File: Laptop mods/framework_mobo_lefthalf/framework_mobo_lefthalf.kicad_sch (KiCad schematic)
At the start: 19 parts

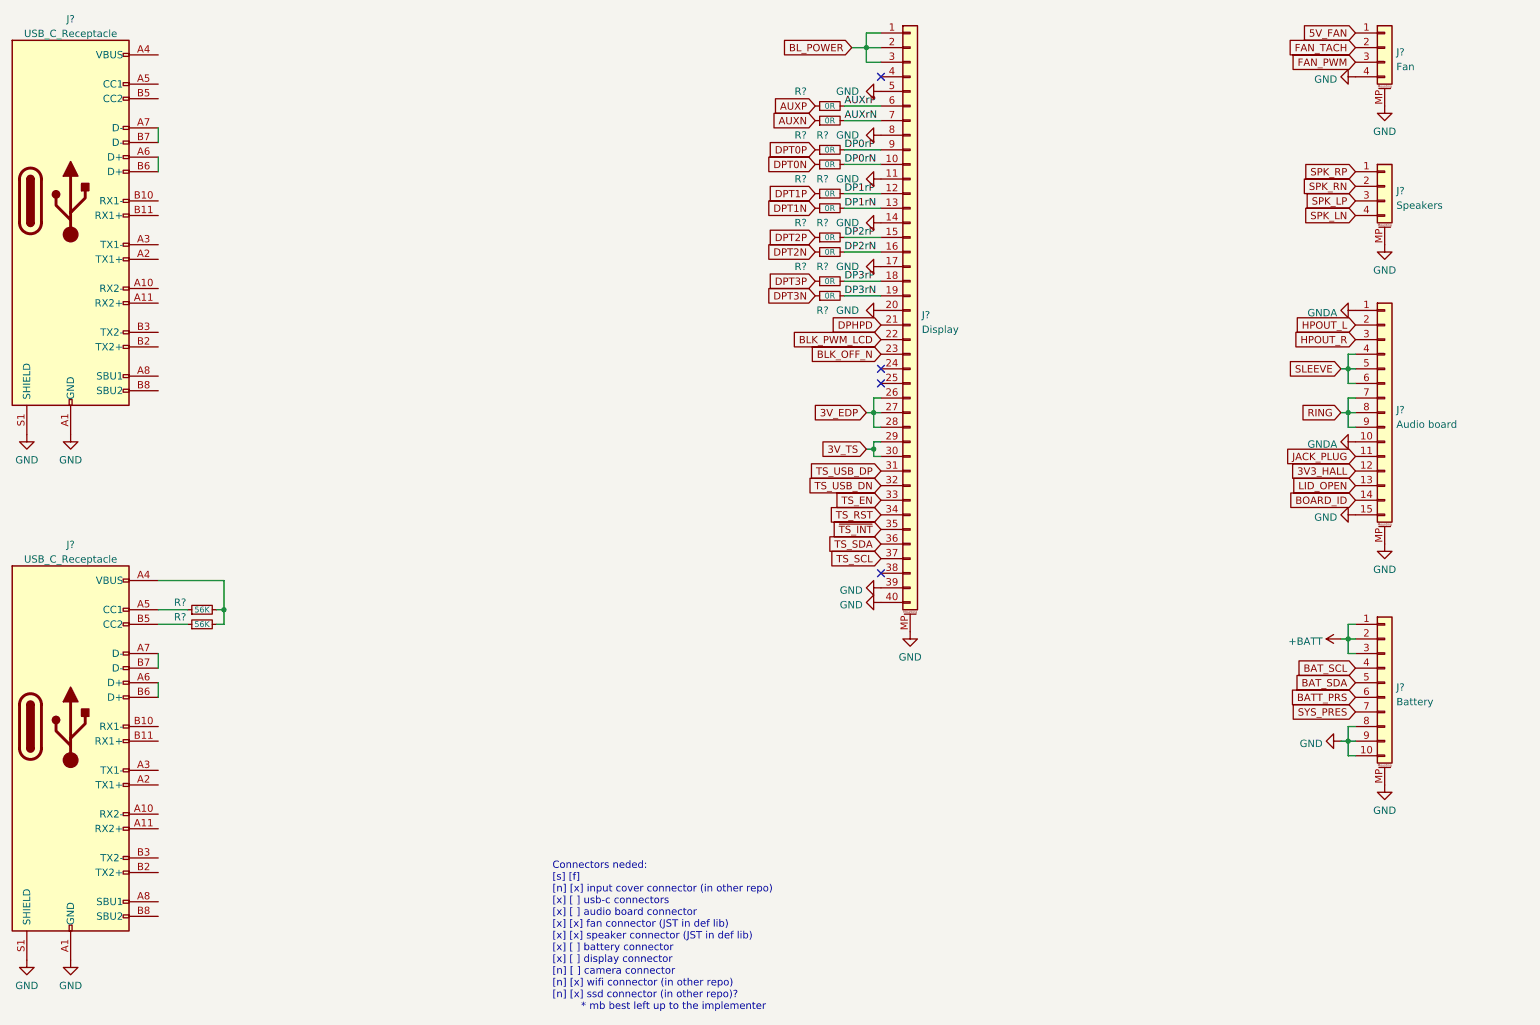
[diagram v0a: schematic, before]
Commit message: framework_mobo_lefthalf: WIP some more, separated stuff into topleft and bottomleft; added display footprint from imnotjames; looking out for any routing hiccups in highspeed stuff. is gonna be 6 layers yay!
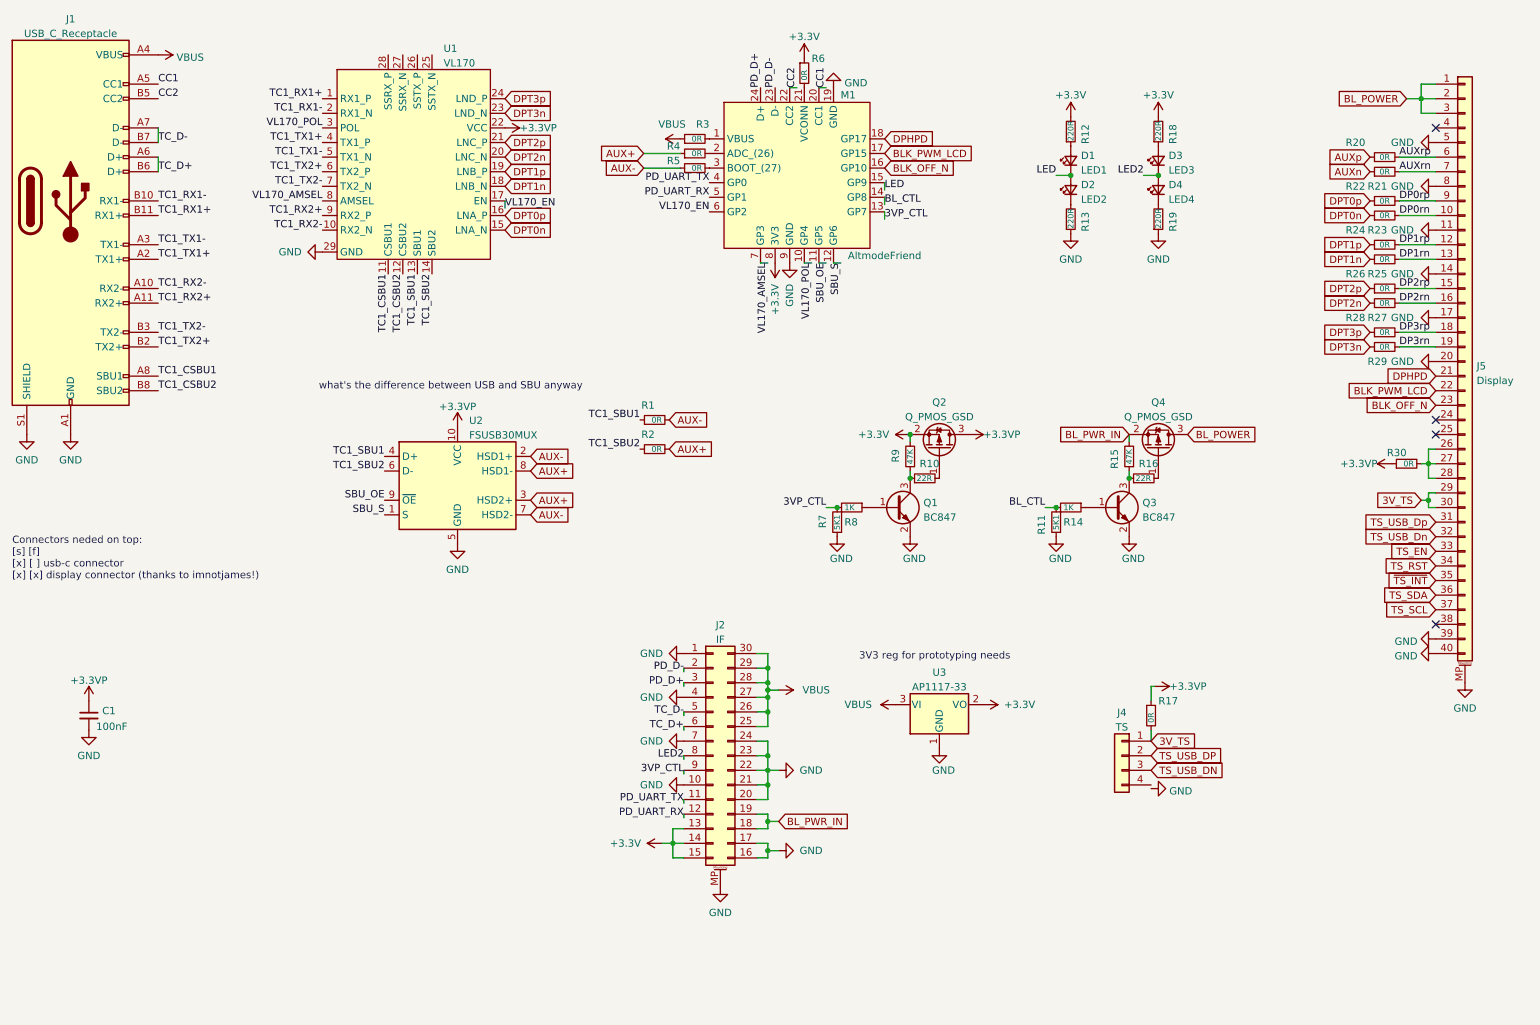
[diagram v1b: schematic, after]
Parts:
- removed J?: Battery, symbol Connector_Generic_MountingPin:Conn_01x10_MountingPin
- removed J?: USB_C_Receptacle, symbol Connector:USB_C_Receptacle
- removed J?: Audio board, symbol Connector_Generic_MountingPin:Conn_01x15_MountingPin
- removed J?: Speakers, symbol Connector_Generic_MountingPin:Conn_01x04_MountingPin
- removed J?: Fan, symbol Connector_Generic_MountingPin:Conn_01x04_MountingPin
- removed R? (x2): 56K, symbol Device:R_Small
- added C1: 100nF, symbol Device:C_Small
- added D1: LED1, symbol Device:LED_Small
- added D2: LED2, symbol Device:LED_Small
- added D3: LED3, symbol Device:LED_Small
- added D4: LED4, symbol Device:LED_Small
- added J2: IF, framework_mobo_lefthalf:FPC_30, symbol Connector_Generic_MountingPin:Conn_02x15_Counter_Clockwise_MountingPin
- added J4: TS, symbol Connector_Generic:Conn_01x04
- added M1: AltmodeFriend, framework_mobo_lefthalf:altmode_friend, symbol altmode_friend:AltmodeFriend
- added Q1, Q3: BC847, symbol Device:Q_NPN_BEC
- added Q2, Q4: Q_PMOS_GSD, symbol Device:Q_PMOS_GSD
- added R1, R17, R2, R3, R30, R4, R5, R6: 0R, symbol Device:R_Small
- added R10, R16: 22R, symbol Device:R_Small
- added R11, R7: 5K1, symbol Device:R_Small
- added R12, R13, R18, R19: 220R, symbol Device:R_Small
- added R14, R8: 1K, symbol Device:R_Small
- added R15, R9: 47K, symbol Device:R_Small
- added U1: VL170, Package_DFN_QFN:QFN-28-1EP_3x6mm_P0.5mm_EP1.7x4.75mm, symbol vl170:VL170
- added U2: FSUSB30MUX, Package_SO:MSOP-10_3x3mm_P0.5mm, symbol Interface_USB:FSUSB30MUX
- added U3: AP1117-33, Package_TO_SOT_SMD:SOT-223-3_TabPin2, symbol Regulator_Linear:AP1117-33
- J1: renamed from J?; footprint (none) -> Connector_USB:USB_C_Receptacle_Amphenol_12401548E4-2A_CircularHoles
- J5: renamed from J?; footprint (none) -> framework_mobo_lefthalf:IPEX_20879-040E-01
- gave numbers to parts that had none: 10
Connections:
- net 3V_TS: now also J4.1 (Pin_1), R17.2
- net BLK_OFF_N: now also M1.16 (GP10)
- net BLK_PWM_LCD: now also M1.17 (GP15)
- net BL_POWER: now also Q4.3 (D)
- net DPHPD: now also M1.18 (GP17)
- net GND: now also C1.2, J2.1 (Pin_1), J2.10 (Pin_10), J2.16 (Pin_16), J2.17 (Pin_17), J2.20 (Pin_20), J2.21 (Pin_21), J2.22 (Pin_22), J2.23 (Pin_23), J2.24 (Pin_24), J2.4 (Pin_4), J2.7 (Pin_7), J2.MP (MountPin), M1.19 (GND), M1.9 (GND), Q1.2 (E), Q3.2 (E), R11.1, R13.1, R19.1, R7.1, U1.29 (GND), U2.5 (GND), U3.1 (GND)
- net TS_USB_DN: now also J4.3 (Pin_3); no longer J5.32 (Pin_32)
- net TS_USB_DP: now also J4.2 (Pin_2); no longer J5.31 (Pin_31)
- net TC1_RX2-: now reaches J1.A10 (RX2-)
- net TC1_RX2-: now also U1.10 (RX2_N)
- net TC1_RX2+: now reaches J1.A11 (RX2+)
- net TC1_RX2+: now also U1.9 (RX2_P)
- net TC1_TX1+: now reaches J1.A2 (TX1+)
- net TC1_TX1+: now also U1.4 (TX1_P)
- net TC1_TX1-: now reaches J1.A3 (TX1-)
- net TC1_TX1-: now also U1.5 (TX1_N)
- net VBUS: now reaches J1.A4 (VBUS), J1.A9 (VBUS), J1.B4 (VBUS), J1.B9 (VBUS)
- net VBUS: now also J2.25 (Pin_25), J2.26 (Pin_26), J2.27 (Pin_27), J2.28 (Pin_28), J2.29 (Pin_29), J2.30 (Pin_30), R3.1, U3.3 (VI)
- net CC1: now reaches J1.A5 (CC1)
- net CC1: now also M1.20 (CC1)
- net TC_D+: now reaches J1.A6 (D+), J1.B6 (D+)
- net TC_D+: now also J2.6 (Pin_6)
- net TC_D-: now reaches J1.A7 (D-), J1.B7 (D-)
- net TC_D-: now also J2.5 (Pin_5)
- net TC1_CSBU1: now reaches J1.A8 (SBU1)
- net TC1_CSBU1: now also U1.11 (CSBU1)
- net TC1_RX1-: now reaches J1.B10 (RX1-)
- net TC1_RX1-: now also U1.2 (RX1_N)
- net TC1_RX1+: now reaches J1.B11 (RX1+)
- net TC1_RX1+: now also U1.1 (RX1_P)
- net TC1_TX2+: now reaches J1.B2 (TX2+)
- net TC1_TX2+: now also U1.6 (TX2_P)
- net TC1_TX2-: now reaches J1.B3 (TX2-)
- net TC1_TX2-: now also U1.7 (TX2_N)
- net CC2: now reaches J1.B5 (CC2)
- net CC2: now also M1.22 (CC2)
- net TC1_CSBU2: now reaches J1.B8 (SBU2)
- net TC1_CSBU2: now also U1.12 (CSBU2)
- net 3V_EDP: no longer names the net of J5.26 (Pin_26), J5.27 (Pin_27), J5.28 (Pin_28)
- net 3V_EDP: now also R30.2
- net AUXN renamed AUXn
- net AUXP renamed AUXp
- net AUXrN renamed AUXrn
- net AUXrP renamed AUXrp
- net DP0rN renamed DP0rn
- net DP0rP renamed DP0rp
- net DP1rN renamed DP1rn
- net DP1rP renamed DP1rp
- net DP2rN renamed DP2rn
- net DP2rP renamed DP2rp
- net DP3rN renamed DP3rn
- net DP3rP renamed DP3rp
- net DPT0N renamed DPT0n
- net DPT0n: now also U1.15 (LNA_N)
- net DPT0P renamed DPT0p
- net DPT0p: now also U1.16 (LNA_P)
- net DPT1N renamed DPT1n
- net DPT1n: now also U1.18 (LNB_N)
- net DPT1P renamed DPT1p
- net DPT1p: now also U1.19 (LNB_P)
- net DPT2N renamed DPT2n
- net DPT2n: now also U1.20 (LNC_N)
- net DPT2P renamed DPT2p
- net DPT2p: now also U1.21 (LNC_P)
- net DPT3N renamed DPT3n
- net DPT3n: now also U1.23 (LND_N)
- net DPT3P renamed DPT3p
- net DPT3p: now also U1.24 (LND_P)
- new net: M1.21 (VCONN), R6.2
- new net: D1.2 (A), R12.1
- new net: Q4.1 (G), R16.2
- new net: Q1.3 (C), R10.1, R9.1
- new net: D3.2 (A), R18.1
- new net: Q3.3 (C), R15.1, R16.1
- new net: M1.2 (ADC_(26)), R4.2
- new net: D2.1 (K), R13.2
- new net: Q1.1 (B), R8.1
- new net: M1.1 (VBUS), R3.2
- new net: M1.3 (BOOT_(27)), R5.2
- new net: D4.1 (K), R19.2
- new net: Q3.1 (B), R14.1
- new net: Q2.1 (G), R10.2
- new net +3.3V: J2.13 (Pin_13), J2.14 (Pin_14), J2.15 (Pin_15), M1.8 (3V3), Q2.2 (S), R12.2, R18.2, R6.1, R9.2, U3.2 (VO)
- new net +3.3VP: C1.1, Q2.3 (D), R17.1, R30.1, U1.22 (VCC), U2.10 (VCC)
- new net 3VP_CTL: J2.9 (Pin_9), M1.13 (GP7), R7.2, R8.2
- new net AUX+: R2.2, R4.1, U2.3 (HSD2+), U2.8 (HSD1-)
- new net AUX-: R1.2, R5.1, U2.2 (HSD1+), U2.7 (HSD2-)
- new net BL_CTL: M1.14 (GP8), R11.2, R14.2
- new net BL_PWR_IN: J2.18 (Pin_18), J2.19 (Pin_19), Q4.2 (S), R15.2
- new net LED: D1.1 (K), D2.2 (A), M1.15 (GP9)
- new net LED2: D3.1 (K), D4.2 (A), J2.8 (Pin_8)
- new net PD_D+: J2.3 (Pin_3), M1.24 (D+)
- new net PD_D-: J2.2 (Pin_2), M1.23 (D-)
- new net PD_UART_RX: J2.12 (Pin_12), M1.5 (GP1)
- new net PD_UART_TX: J2.11 (Pin_11), M1.4 (GP0)
- new net SBU_OE: M1.11 (GP5), U2.9 (~{OE})
- new net SBU_S: M1.12 (GP6), U2.1 (S)
- new net TC1_SBU1: R1.1, U1.13 (SBU1), U2.4 (D+)
- new net TC1_SBU2: R2.1, U1.14 (SBU2), U2.6 (D-)
- new net TS_USB_Dn: J5.32 (Pin_32)
- new net TS_USB_Dp: J5.31 (Pin_31)
- new net VL170_AMSEL: M1.7 (GP3), U1.8 (AMSEL)
- new net VL170_EN: M1.6 (GP2), U1.17 (EN)
- new net VL170_POL: M1.10 (GP4), U1.3 (POL)
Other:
- note added: "3V3 reg for prototyping needs"
- note added: "Connectors neded on top: [s] [f] [x] [ ] usb-c connector [x] [x] display connector (thanks to imnotjames!)"
- note added: "what's the difference between USB and SBU anyway"
- note removed: "Connectors neded: [s] [f] [n] [x] input cover connector (in other repo) [x] [ ] usb-c connectors [x] [ ] audio board connector [x] [x] fan connector (JST in def lib) [x] [x] speaker connector (JST in def lib) [x] [ ] battery connector [x] [ ] display connector [n] [ ] camera connector [n] [x] wifi connector (in other repo) [n] [x] ssd connector (in other repo)? * mb best left up to the implementer"
- moved on the sheet: J5, R20, R21, R22, R23, R24, R25, R26, R27, R28, R29

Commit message: framework_mobo_lefthalf: v2 as ordered, not tested yet
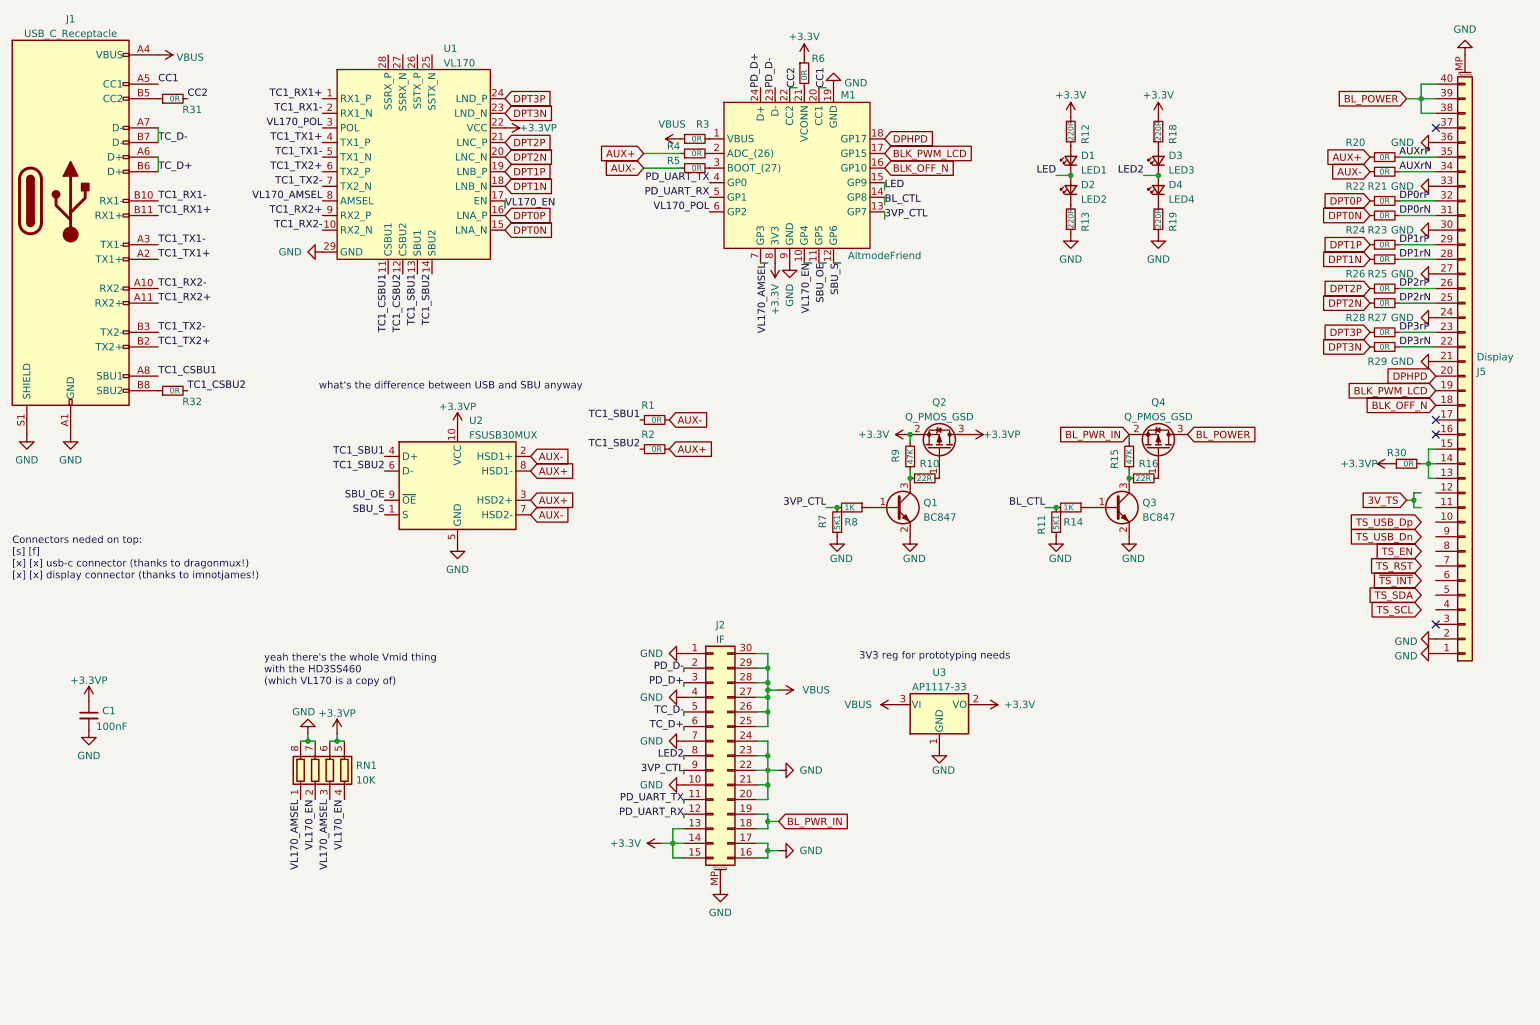
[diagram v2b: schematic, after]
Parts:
- removed J4: TS, symbol Connector_Generic:Conn_01x04
- removed R17: 0R, symbol Device:R_Small
- added R31, R32: 0R, Resistor_SMD:R_0603_1608Metric, symbol Device:R_Small
- added RN1: 10K, symbol Device:R_Pack04
- C1: footprint (none) -> Capacitor_SMD:C_0603_1608Metric
- D1, D2, D3, D4: footprint (none) -> LED_SMD:LED_0603_1608Metric
- J1: footprint Connector_USB:USB_C_Receptacle_Amphenol_12401548E4-2A_CircularHoles -> framework_mobo_lefthalf:USB-3.1-Type-C_In-PCB
- Q1, Q2, Q3, Q4: footprint (none) -> Package_TO_SOT_SMD:SOT-23
- R1, R10, R2, R20, R21, R22, R23, R24, R25, R26, R27, R28, R29, R3, R4, R5: footprint (none) -> Resistor_SMD:R_0402_1005Metric
- R11, R12, R13, R14, R15, R16, R18, R19, R6, R7, R8, R9: footprint (none) -> Resistor_SMD:R_0603_1608Metric
- R30: footprint (none) -> Resistor_SMD:R_0805_2012Metric
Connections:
- net AUXn is gone; now on net AUX-: R21.1
- net AUXp is gone; now on net AUX+: R20.1
- net +3.3VP: now also RN1.5 (R4.2), RN1.6 (R3.2)
- net 3V_TS: no longer J5.29 (Pin_29), J5.30 (Pin_30)
- net BLK_OFF_N: now also J5.18 (Pin_18); no longer J5.23 (Pin_23)
- net BLK_PWM_LCD: now also J5.19 (Pin_19); no longer J5.22 (Pin_22)
- net BL_POWER: now also J5.38 (Pin_38), J5.39 (Pin_39), J5.40 (Pin_40); no longer J5.1 (Pin_1), J5.2 (Pin_2), J5.3 (Pin_3)
- net CC2: now also R31.2; no longer J1.B5 (CC2)
- net DPHPD: now also J5.20 (Pin_20); no longer J5.21 (Pin_21)
- net GND: now also J5.1 (Pin_1), J5.2 (Pin_2), J5.21 (Pin_21), J5.24 (Pin_24), J5.27 (Pin_27), J5.30 (Pin_30), J5.33 (Pin_33), J5.36 (Pin_36), RN1.7 (R2.2), RN1.8 (R1.2); no longer J5.11 (Pin_11), J5.14 (Pin_14), J5.17 (Pin_17), J5.20 (Pin_20), J5.39 (Pin_39), J5.40 (Pin_40), J5.5 (Pin_5), J5.8 (Pin_8)
- net TC1_CSBU2: now also R32.2; no longer J1.B8 (SBU2)
- net TS_EN: no longer J5.33 (Pin_33)
- net TS_RST: no longer J5.34 (Pin_34)
- net TS_SCL: no longer J5.37 (Pin_37)
- net TS_SDA: no longer J5.36 (Pin_36)
- net TS_USB_Dn: no longer J5.32 (Pin_32)
- net TS_USB_Dp: no longer J5.31 (Pin_31)
- net VL170_AMSEL: now also RN1.1 (R1.1), RN1.3 (R3.1)
- net VL170_EN: now also M1.10 (GP4), RN1.2 (R2.1), RN1.4 (R4.1); no longer M1.6 (GP2)
- net VL170_POL: now also M1.6 (GP2); no longer M1.10 (GP4)
- net ~{TS_INT}: no longer J5.35 (Pin_35)
- net DP2rN: now reaches J5.25 (Pin_25)
- net DP2rN: now also R27.2
- net AUXrn: no longer names the net of J5.7 (Pin_7)
- net AUXrn: no longer R21.2
- net AUXrp: no longer names the net of J5.6 (Pin_6)
- net AUXrp: no longer R20.2
- net DP0rn: no longer names the net of J5.10 (Pin_10)
- net DP0rn: no longer R23.2
- net DP0rp: no longer names the net of J5.9 (Pin_9)
- net DP0rp: no longer R22.2
- net DP1rn: no longer names the net of J5.13 (Pin_13)
- net DP1rn: now also J5.14 (Pin_14), J5.15 (Pin_15), R30.2; no longer R25.2
- net DP1rp: no longer names the net of J5.12 (Pin_12)
- net DP1rp: no longer R24.2
- net DP2rn: no longer names the net of J5.16 (Pin_16)
- net DP2rn: no longer R27.2
- net DP2rp renamed DP2rP
- net DP2rP: now also J5.26 (Pin_26); no longer J5.15 (Pin_15)
- net DP3rn renamed DP3rN
- net DP3rN: now also J5.22 (Pin_22); no longer J5.19 (Pin_19)
- net DP3rp renamed DP3rP
- net DP3rP: now also J5.23 (Pin_23); no longer J5.18 (Pin_18)
- net DPT0n renamed DPT0N
- net DPT0p renamed DPT0P
- net DPT1n renamed DPT1N
- net DPT1p renamed DPT1P
- net DPT2n renamed DPT2N
- net DPT2p renamed DPT2P
- net DPT3n renamed DPT3N
- net DPT3p renamed DPT3P
- new net: J1.B5 (CC2), R31.1
- new net: J1.B8 (SBU2), R32.1
- new net AUXrN: J5.34 (Pin_34), R21.2
- new net AUXrP: J5.35 (Pin_35), R20.2
- new net DP0rN: J5.31 (Pin_31), R23.2
- new net DP0rP: J5.32 (Pin_32), R22.2
- new net DP1rN: J5.28 (Pin_28), R25.2
- new net DP1rP: J5.29 (Pin_29), R24.2
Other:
- note added: "Connectors neded on top: [s] [f] [x] [x] usb-c connector (thanks to dragonmux!) [x] [x] display connector (thanks to imnotjames!)"
- note added: "yeah there's the whole Vmid thing with the HD3SS460 (which VL170 is a copy of)"
- note removed: "Connectors neded on top: [s] [f] [x] [ ] usb-c connector [x] [x] display connector (thanks to imnotjames!)"
- moved on the sheet: J5
